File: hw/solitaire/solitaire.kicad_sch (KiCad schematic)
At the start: 0 parts

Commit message: Add TPS63900 datasheet and register coil/MCU/nav-switch KiCad libraries
Adds symbol/footprint packages for the DFE201612E inductor, MSP430FR2355TDBTR,
and Alps SKQUCAA010 5-way nav switch, wired up via sym-lib-table/fp-lib-table.
Ignores KiCad's auto-generated backups directory.

Co-Authored-By: Claude Sonnet 5 <noreply@anthropic.com>
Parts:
- added C1: 22uF, symbol Device:C_Polarized_US
- added C2: 10uF, symbol Device:C_Polarized_US
- added J1: Conn_01x10, symbol Connector_Generic:Conn_01x10
- added J2: SKQUCAA010, CONN_SKQUC_ALPS, symbol SKQUCAA010:SKQUCAA010
- added L1: 2.2 uh, symbol coil:DFE201612E-2R2M=P2
- added R1: 2.74, symbol Device:R_Small
- added R2: 10.5, symbol Device:R_Small
- added R3: 13.3, symbol Device:R_Small
- added U1: TPS63900, Package_SON:WSON-10-1EP_2.5x2.5mm_P0.5mm_EP1.2x2mm_ThermalVias, symbol Regulator_Switching:TPS63900
- added U2: MSP430FR2355TDBTR, symbol MSP430FR2355:MSP430FR2355TDBTR
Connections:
- new net: L1.1, U1.9 (LX1)
- new net: L1.2, U1.7 (LX2)
- new net: R2.1, U1.3 (CFG1)
- new net: R1.1, U1.4 (CFG2)
- new net: R3.1, U1.5 (CFG3)
- new net +3V0: C2.1, U1.1 (EN), U1.10 (VIN), U1.2 (SEL)
- new net GND: R1.2, R2.2, R3.2, U1.11 (GND), U1.8 (GND), U2.11 (DVSS)
- new net VCC: C1.1, U1.6 (VOUT), U2.10 (DVCC)

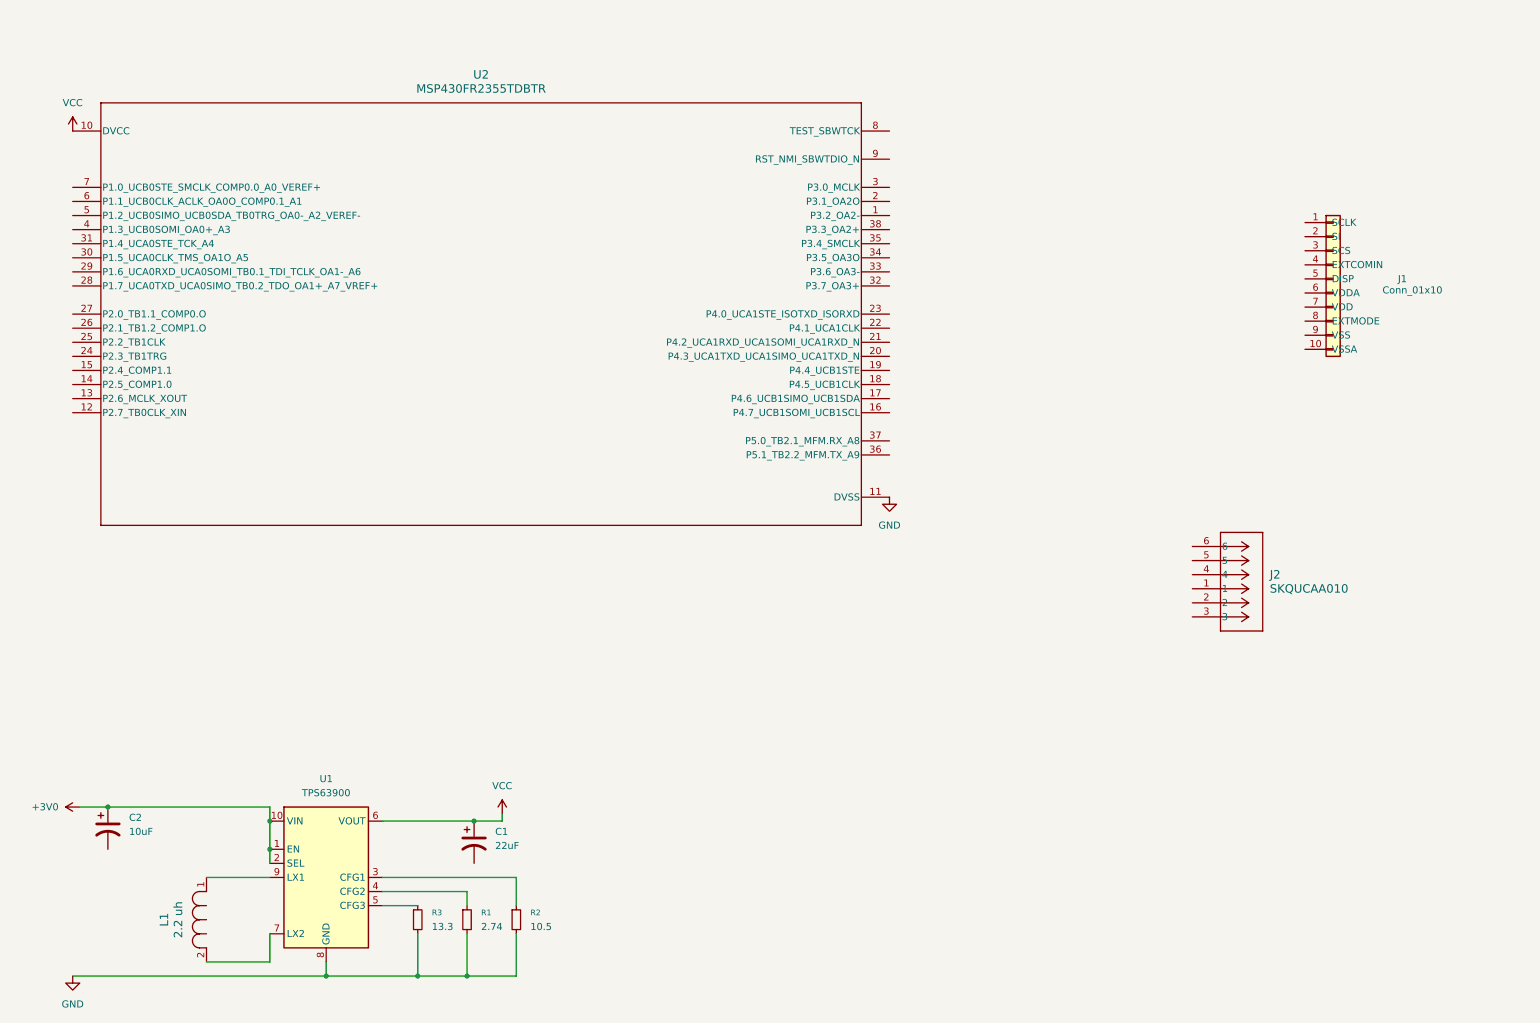
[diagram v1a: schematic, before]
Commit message: Add PWR_FLAG symbols and no-connect flags to clean up ERC
Adds PWR_FLAG on +BATT and GND nets (both are externally driven by
the battery, with no local power-output pin) and no-connect flags on
spare MSP430 GPIOs and U2 pin 1 (P3.2_OA2-). ERC down from 56 to 31
violations, with only 2 errors remaining (mislabeled LX1/LX2 pin
types in the imported TPS63900 symbol, not a wiring issue).

Co-Authored-By: Claude Sonnet 5 <noreply@anthropic.com>
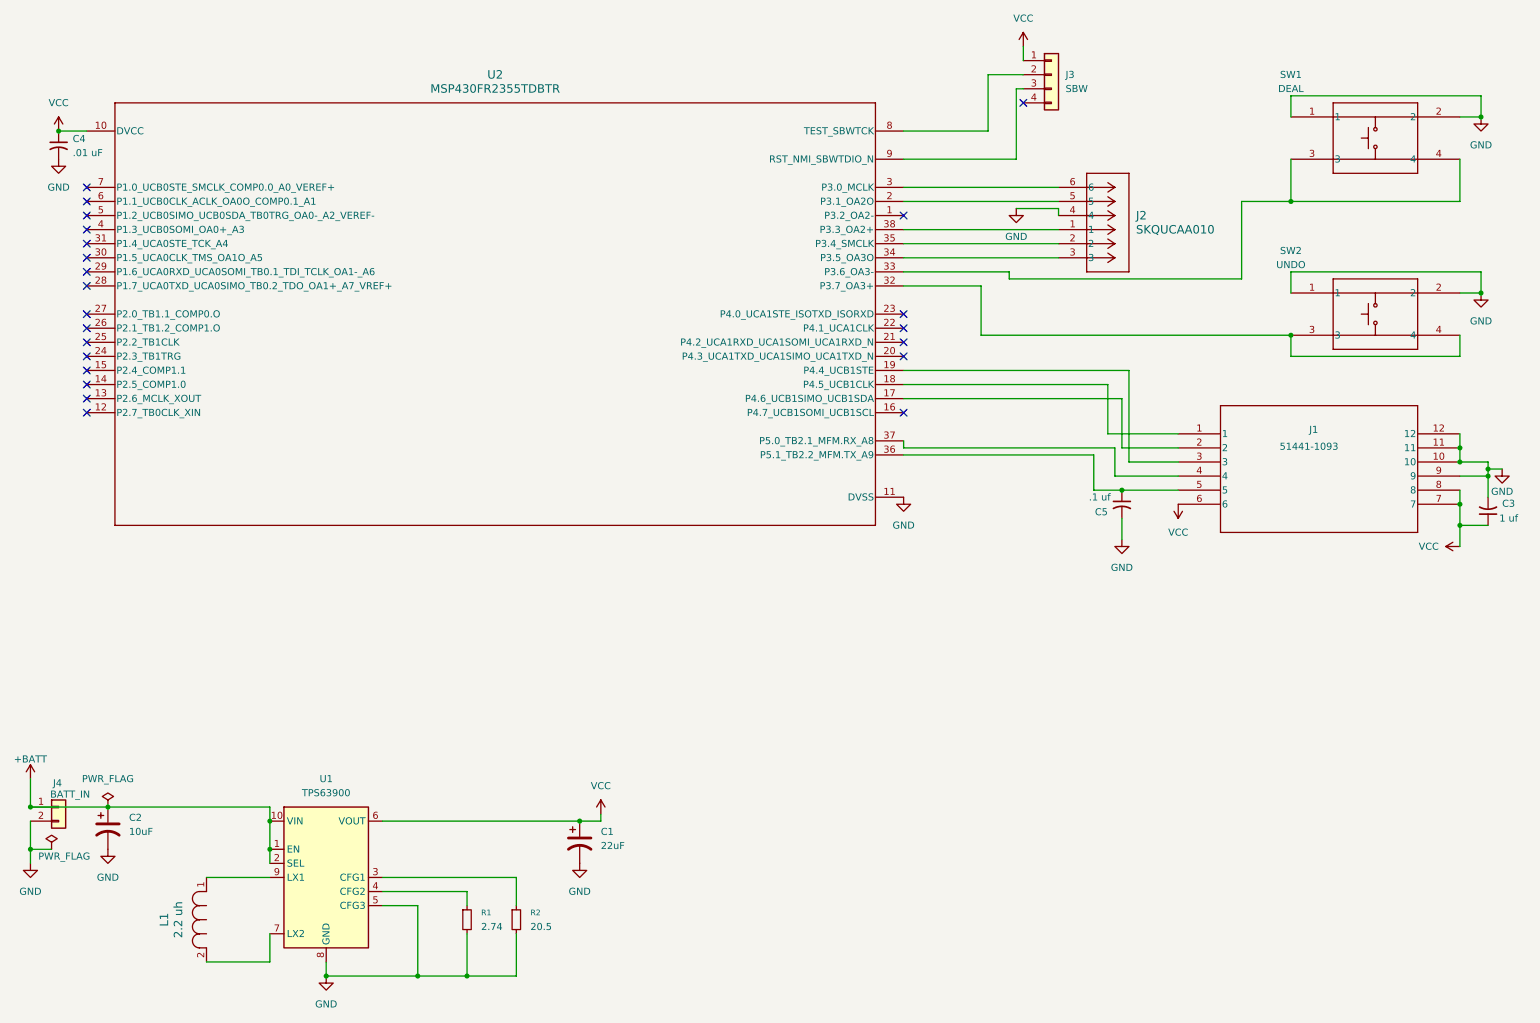
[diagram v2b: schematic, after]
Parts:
- removed R3: 13.3, symbol Device:R_Small
- added C3: 1 uf, Capacitor_SMD:C_0603_1608Metric, symbol Device:C_Small_US
- added C4: .01 uF, Capacitor_SMD:C_0603_1608Metric, symbol Device:C_Small_US
- added C5: .1 uf, Capacitor_SMD:C_0603_1608Metric, symbol Device:C_Small_US
- added J3: SBW, Connector_PinHeader_2.54mm:PinHeader_1x04_P2.54mm_Vertical, symbol Connector_Generic:Conn_01x04
- added J4: BATT_IN, Connector_JST:JST_PH_S2B-PH-K_1x02_P2.00mm_Horizontal, symbol Connector_Generic:Conn_01x02
- added SW1: DEAL, SKRPACE010:SW_SKRPACE010_AAL, symbol SKRPACE010:SKRPACE010
- added SW2: UNDO, SKRPACE010:SW_SKRPACE010_AAL, symbol SKRPACE010:SKRPACE010
- C1, C2: footprint (none) -> Capacitor_SMD:C_0603_1608Metric
- J1: value Conn_01x10 -> 51441-1093; footprint (none) -> 514411093:CON10_1X10_DRB_51441_MOL; symbol Connector_Generic:Conn_01x10 -> 514411093:514411093
- J2: footprint CONN_SKQUC_ALPS -> SKQUCAA010:CONN_SKQUC_ALPS
- L1: footprint (none) -> coil:IND_DFE2016_MUR
- R1: footprint (none) -> Resistor_SMD:R_0603_1608Metric
- R2: value 10.5 -> 20.5; footprint (none) -> Resistor_SMD:R_0603_1608Metric
- U2: footprint (none) -> MSP430FR2355TDBTR:DBT0038A_L
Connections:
- net GND: now also C1.2, C2.2, J1.10, J1.11, J1.12, J1.9, J2.4, U1.5 (CFG3), C3.2, C4.2, C5.2, J4.2 (Pin_2), SW1.1, SW1.2, SW2.1, SW2.2
- net VCC: now also J1.6, J1.7, J1.8, C3.1, C4.1, J3.1 (Pin_1)
- net at J2.1: now also U2.38 (P3.3_OA2+)
- net at J2.2: now also U2.35 (P3.4_SMCLK)
- net at J2.3: now also U2.34 (P3.5_OA3O)
- net at J2.5: now also U2.2 (P3.1_OA2O)
- net at J2.6: now also U2.3 (P3.0_MCLK)
- net at U2.17 (P4.6_UCB1SIMO_UCB1SDA): now also J1.2
- net at U2.18 (P4.5_UCB1CLK): now also J1.1
- net at U2.19 (P4.4_UCB1STE): now also J1.3
- net at U2.32 (P3.7_OA3+): now also SW2.3, SW2.4
- net at U2.33 (P3.6_OA3-): now also SW1.3, SW1.4
- net at U2.36 (P5.1_TB2.2_MFM.TX_A9): now also J1.5, C5.1
- net at U2.37 (P5.0_TB2.1_MFM.RX_A8): now also J1.4
- net at U2.8 (TEST_SBWTCK): now also J3.2 (Pin_2)
- net at U2.9 (RST_NMI_SBWTDIO_N): now also J3.3 (Pin_3)
- net +3V0 renamed +BATT
- net +BATT: now also J4.1 (Pin_1)
- no-connect marks 0 -> 23
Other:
- moved on the sheet: C1, J2, U2

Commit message: Rename nav switch J2->SW3, add direction net labels, document case dimensions
Renamed the SKQUCAA010 nav switch reference from J2 (Ultra Librarian's
default connector prefix) to SW3 to match the SW1/SW2 naming convention,
and added NAV_UP/DOWN/LEFT/RIGHT/CENTER net labels on its schematic pins
so the up/down/left/right mapping is legible without cross-referencing
the datasheet.

Also adds docs/case_design_dimensions.md: verified component positions
and mechanical envelopes pulled from datasheets for FreeCAD case design,
including nav switch stem geometry/pivot point for sizing a knob cutout
and the selected 2xAA battery holder (Adafruit #4194).

Co-Authored-By: Claude Sonnet 5 <noreply@anthropic.com>
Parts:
- renumbered J2 to SW3
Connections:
- net NAV_UP: now reaches SW3.1, U2.38 (P3.3_OA2+)
- net NAV_LEFT: now reaches SW3.2, U2.35 (P3.4_SMCLK)
- net NAV_DOWN: now reaches SW3.3, U2.34 (P3.5_OA3O)
- net NAV_RIGHT: now reaches SW3.5, U2.2 (P3.1_OA2O)
- net NAV_CENTER: now reaches SW3.6, U2.3 (P3.0_MCLK)
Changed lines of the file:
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@@
+		)
+	)
+	(label "NAV_CENTER"
+		(at 176 44.45 0)
+		(effects
+			(font
+				(size 1.27 1.27)
+			)
+			(justify left bottom)
 		)
 	)
@@
 		)
 	)
+	(label "NAV_DOWN"
+		(at 176 57.15 0)
+		(effects
+			(font
+				(size 1.27 1.27)
+			)
+			(justify left bottom)
+		)
+	)
 	(wire
 		(pts
@@
 		)
 	)
+	(label "NAV_RIGHT"
+		(at 176 46.99 0)
+		(effects
+			(font
+				(size 1.27 1.27)
+			)
+			(justify left bottom)
+		)
+	)
 	(wire
 		(pts
@@
 		)
 	)
+	(label "NAV_LEFT"
+		(at 176 54.61 0)
+		(effects
+			(font
+				(size 1.27 1.27)
+			)
+			(justify left bottom)
+		)
+	)
 	(wire
 		(pts
@@
 			(width 0)
 			(type default)
+		)
+	)
+	(label "NAV_UP"
+		(at 176 52.07 0)
+		(effects
+			(font
+				(size 1.27 1.27)
+			)
+			(justify left bottom)
 		)
 	)
@@
 		(dnp no)
 		(fields_autoplaced yes)
-		(property "Reference" "J2"
+		(property "Reference" "SW3"
 			(at 214.63 49.5299 0)
 			(effects
@@
 			(project ""
 				(path "/37bed383-82de-493d-be12-9430e997c33d"
-					(reference "J2")
+					(reference "SW3")
 					(unit 1)
 				)

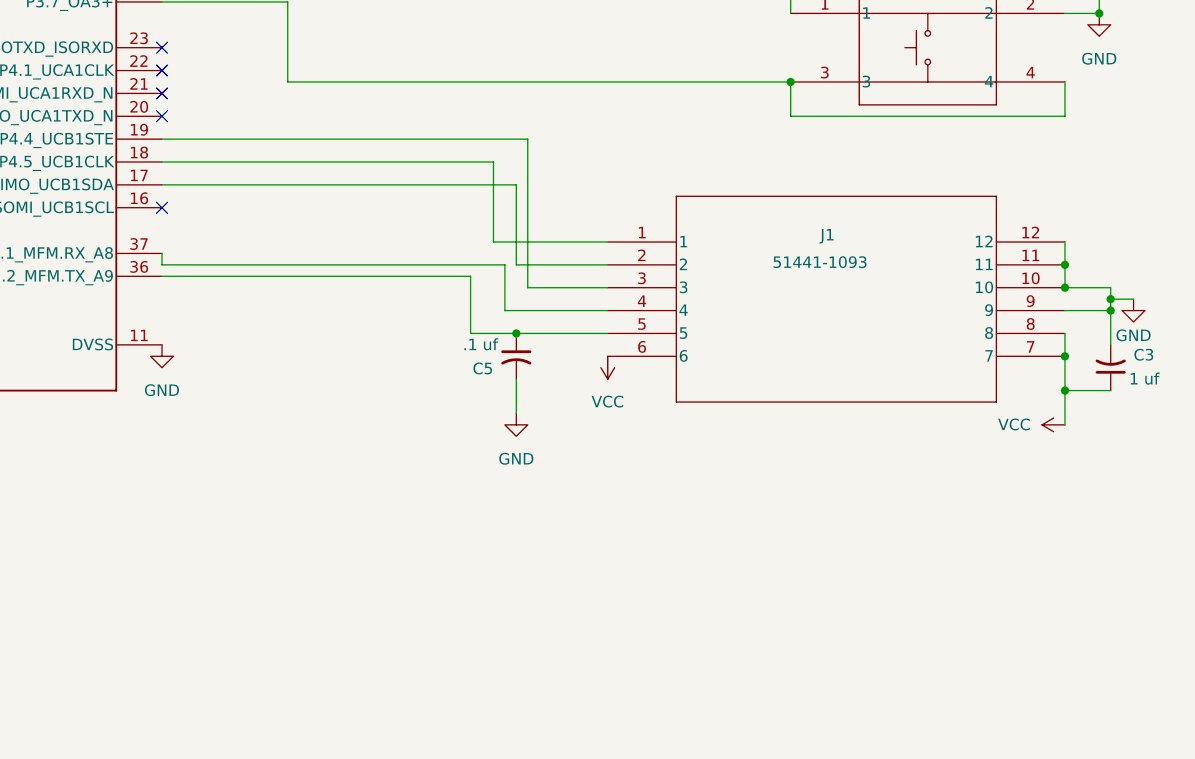
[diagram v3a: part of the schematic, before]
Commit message: Re-swap J1 to GCT FFC2B35-10-T, fill GND plane, fix DRC/ERC violations
Redoes the obsolete-Molex-to-GCT J1 connector swap (previously reverted
in bc0f137) with fresh EDA files from JLCPCB, and ties up the loose ends
that were left dangling mid-edit:

- J1 pins 11/12 (mechanical/shield pads) were floating with no net,
  sitting directly on GND copper - added the pins to the FFC2B35-10-T
  symbol (embedded copy + external .kicad_sym), wired them to a new
  GND flag, and set the matching PCB pads to the GND net. Fixes 2
  shorting_items, 1 clearance, 1 hole_clearance, and 4 solder_mask_bridge
  DRC violations.
- The B.Cu GND zone existed but had never been filled, fragmenting the
  ground net into disconnected islands. Filled it, resolving 12 dangling
  vias and 12 missing-connection DRC warnings.
- J1's silkscreen reference was clipped by its own solder mask - moved
  it below the connector body.

kicad-cli pcb drc: 23 violations + 12 unconnected -> 0/0.
kicad-cli sch erc: same 31-warning baseline plus the expected
"unspecified pintype" nags for the 2 new pins - no new genuine errors.

Co-Authored-By: Claude Sonnet 5 <noreply@anthropic.com>
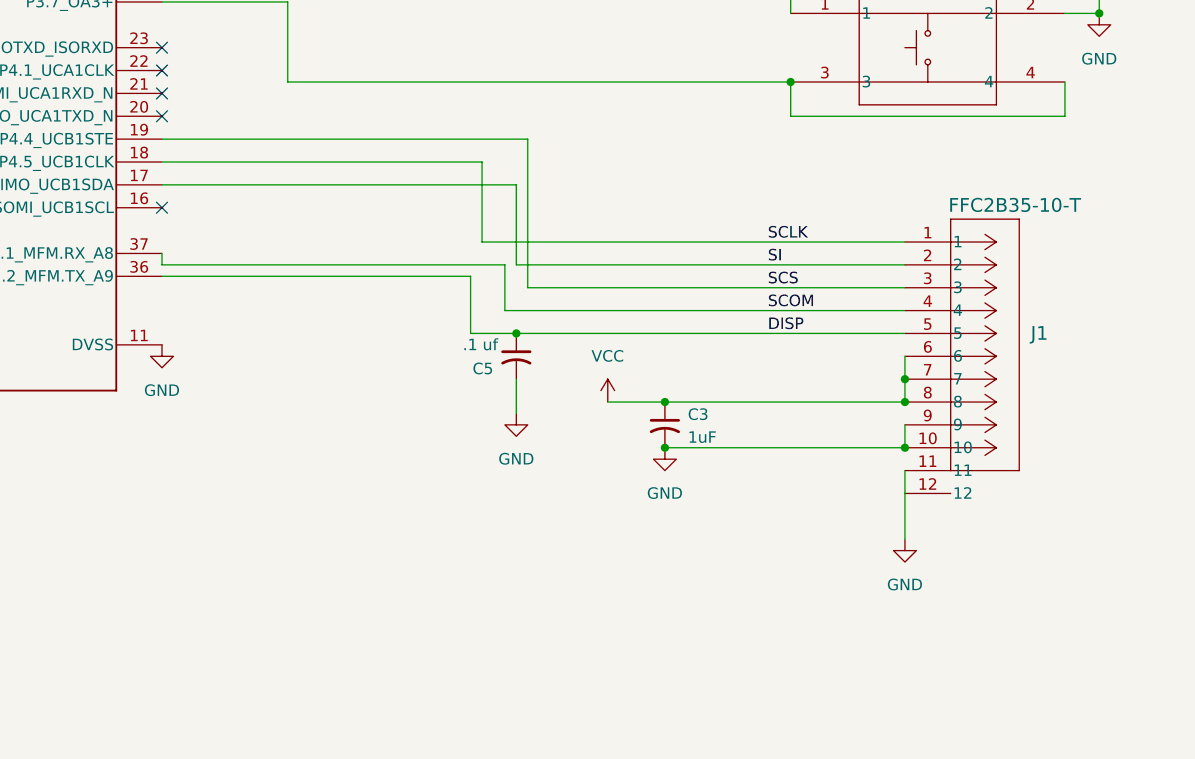
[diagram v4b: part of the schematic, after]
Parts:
- removed J1: 51441-1093, 514411093:CON10_1X10_DRB_51441_MOL, symbol 514411093:514411093
- added J1: FFC2B35-10-T, CONN_FFC2B35-10-x_GCT, symbol disp_connector:FFC2B35-10-T
- C3: value 1 uf -> 1uF
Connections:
- net GND: now also J1.10, J1.11, J1.12, J1.9
- net VCC: now also J1.6, J1.7, J1.8
- net DISP: now reaches C5.1, U2.36 (P5.1_TB2.2_MFM.TX_A9)
- net DISP: now also J1.5
- net SI: now reaches U2.17 (P4.6_UCB1SIMO_UCB1SDA)
- net SI: now also J1.2
- net SCLK: now reaches U2.18 (P4.5_UCB1CLK)
- net SCLK: now also J1.1
- net SCS: now reaches U2.19 (P4.4_UCB1STE)
- net SCS: now also J1.3
- net SCOM: now reaches U2.37 (P5.0_TB2.1_MFM.RX_A8)
- net SCOM: now also J1.4
